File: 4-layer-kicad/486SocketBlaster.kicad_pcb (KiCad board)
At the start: 4 copper layers, 47.6 x 51.8 mm, 18 parts, among them U1 TPS563200

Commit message: update
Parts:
- added R4: 40.2K, 486SocketBlaster:R_0603_1608Metric, F.Cu at (130.6, 52.6)
- added RV1: 100K, 486SocketBlaster:tinySMDpot, F.Cu at (128.0, 46.2)
- R2: value 33.2K -> 68K
- moved C7 4.44 mm to (121.5, 44.2)
- moved C5 1.31 mm to (117.7, 44.2)
- moved C6 1.31 mm to (114.0, 44.2)
- moved C2 1.13 mm to (130.6, 62.3)
- moved L1 1.02 mm to (115.6, 55.1)
- moved R2 1.02 mm to (127.4, 52.6)
- moved R3 1.02 mm to (124.2, 52.6)
- moved C4 1.02 mm to (130.6, 57.7)
- moved R1 1.02 mm to (127.4, 57.7)
- moved U1 1.02 mm to (123.1, 57.7)
- moved C1 0.81 mm to (127.4, 62.3)
- moved C3 0.56 mm to (124.2, 62.3)
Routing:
- net Vin: track 15.9 -> 0.00 mm, vias 12 -> 6
- net Net-(RV1-Pad2): track 0.00 -> 5.18 mm
- net Vout: track 3.80 -> 8.05 mm, vias 8 -> 6
- net FBVoltage: track 10.6 -> 14.3 mm

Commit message: update
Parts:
- moved R4 15.8 mm to (115.2, 56.2)
- moved R2 15.7 mm to (112.1, 56.2)
- moved RV1 13.7 mm to (114.9, 50.2), turned to -90 degrees
- moved C2 12.8 mm to (117.9, 61.2)
- moved C1 12.8 mm to (114.7, 61.2)
- moved L1 9.99 mm to (125.5, 54.4)
- moved C7 9.78 mm to (131.3, 44.2)
- moved C5 9.78 mm to (127.5, 44.2)
- moved C6 9.78 mm to (123.8, 44.2)
- moved R3 6.79 mm to (118.5, 56.2)
- moved U1 4.49 mm to (125.5, 61.4), turned to -90 degrees
- moved C3 3.54 mm to (120.9, 61.2)
- moved R1 3.38 mm to (130.3, 55.9)
- moved C4 2.43 mm to (130.3, 60.1)
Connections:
- net Net-(RV1-Pad2) renamed /Trim
- C4 pad 1: SW -> Net-(U1-Pad6)
- C4 pad 2: Net-(C4-Pad2) -> /SW
- L1 pad 1: SW -> /SW
- R1 pad 1: Vin -> Net-(U1-Pad5)
- R1 pad 2: Net-(R1-Pad2) -> Vin
- R2 pad 1: FBVoltage -> /FBVoltage
- R3 pad 1: GND -> /FBVoltage
- R3 pad 2: FBVoltage -> GND
- R4 pad 1: FBVoltage -> /FBVoltage
- RV1 pad 1: Vout -> unconnected-(RV1-Pad1)
- RV1 pad 3: unconnected-(RV1-Pad3) -> Vout
- U1 pad 2: SW -> /SW
- U1 pad 4: FBVoltage -> /FBVoltage
- U1 pad 5: Net-(R1-Pad2) -> Net-(U1-Pad5)
- U1 pad 6: Net-(C4-Pad2) -> Net-(U1-Pad6)
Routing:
- net /FBVoltage: track 0.00 -> 28.0 mm
- net SW: track 24.6 -> 0.00 mm, vias 2 -> 0
- net Net-(U1-Pad5): track 0.00 -> 14.6 mm
- net FBVoltage: track 14.3 -> 0.00 mm, vias 2 -> 0
- net Net-(C4-Pad2): track 7.11 -> 0.00 mm
- net /SW: track 0.00 -> 6.05 mm
- net Net-(U1-Pad6): track 0.00 -> 5.04 mm
- net Vout: track 8.05 -> 4.26 mm, vias 6 -> 5
- net Net-(R1-Pad2): track 3.50 -> 0.00 mm
- net GND: track 8.60 -> 6.39 mm, vias 8 -> 10
- net Net-(Pins1-PadE3): track 3.68 -> 1.84 mm
- net Net-(Pins1-PadQ16): track 3.68 -> 1.84 mm
- net Net-(Pins1-PadQ14): track 3.53 -> 1.69 mm
- net Net-(Pins1-PadN16): track 3.68 -> 1.84 mm
- net Net-(Pins1-PadE15): track 3.68 -> 1.84 mm
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- added copper zone on F.Cu, net /SW
- added copper zone on B.Cu, net Vout
- removed copper zone on F.Cu, net SW
- removed copper zone on In1.Cu, net Vout

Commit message: update
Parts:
- added C8: 10uf, 486SocketBlaster:C_0805_2012Metric, F.Cu at (131.7, 44.1)
- added G***: LOGO, 486SocketBlaster:ScrapComputinglogo, B.Cu at (127.8, 58.7)
- added G***: LOGO, 486SocketBlaster:lime_logo_9mm, B.Cu at (114.9, 58.7)
- C3, C4: footprint 486SocketBlaster:C_0603_1608Metric -> 486SocketBlaster:C_0805_2012Metric
- C7: value 47uf -> 10uf; footprint 486SocketBlaster:CP_EIA-3216-12_Kemet-S_Pad1.58x1.35mm_HandSolder -> 486SocketBlaster:C_0805_2012Metric
- R2: value 68K -> 68.1K
- moved C7 10.9 mm to (120.4, 44.1)
- moved RV1 1.00 mm to (113.9, 50.2)
- moved C1 0.71 mm to (114.0, 61.2)
- moved C2 0.58 mm to (117.3, 61.2)
- moved C5 0.38 mm to (127.9, 44.2)
- moved C6 0.38 mm to (124.2, 44.2)
- moved C3 0.33 mm to (120.5, 61.2)
- moved Pins1 0.25 mm to (142.0, 31.8)
- renumbered CLKMUL1 to CLKMUL
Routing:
- net /FBVoltage: track 28.0 -> 23.6 mm
- net Vout: track 4.26 -> 3.85 mm, vias 5 -> 7
- net GND: track 6.39 -> 6.24 mm, vias 10 -> 11
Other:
- board text added: "/"
- board text added: "2.7v"
- board text added: "4.3v"
- board text added: "=>"
- board text added: "A"
- board text added: "Big Thanks:"
- board text added: "CalamityLime"
- board text added: "DX"
- board text added: "DX2"
- board text added: "N"
- board text added: "NC"
- board text added: "On-Board Regulator Edition"
- board text added: "On-Board Regulator:"
- board text added: "Original Design:"
- board text added: "OxCats"
- board text added: "SET BY MOTHERBOARD"
- board text added: "ScrapComputing"
- board text removed: "+"
- board text removed: "."
- board text removed: "DX/DX2"
- board text removed: "N/A"
- board text removed: "N/C"
- board text removed: "Set by Motherboard"
- board text removed: "by ScrapComputing"
- board text removed: "rev0.Lime"

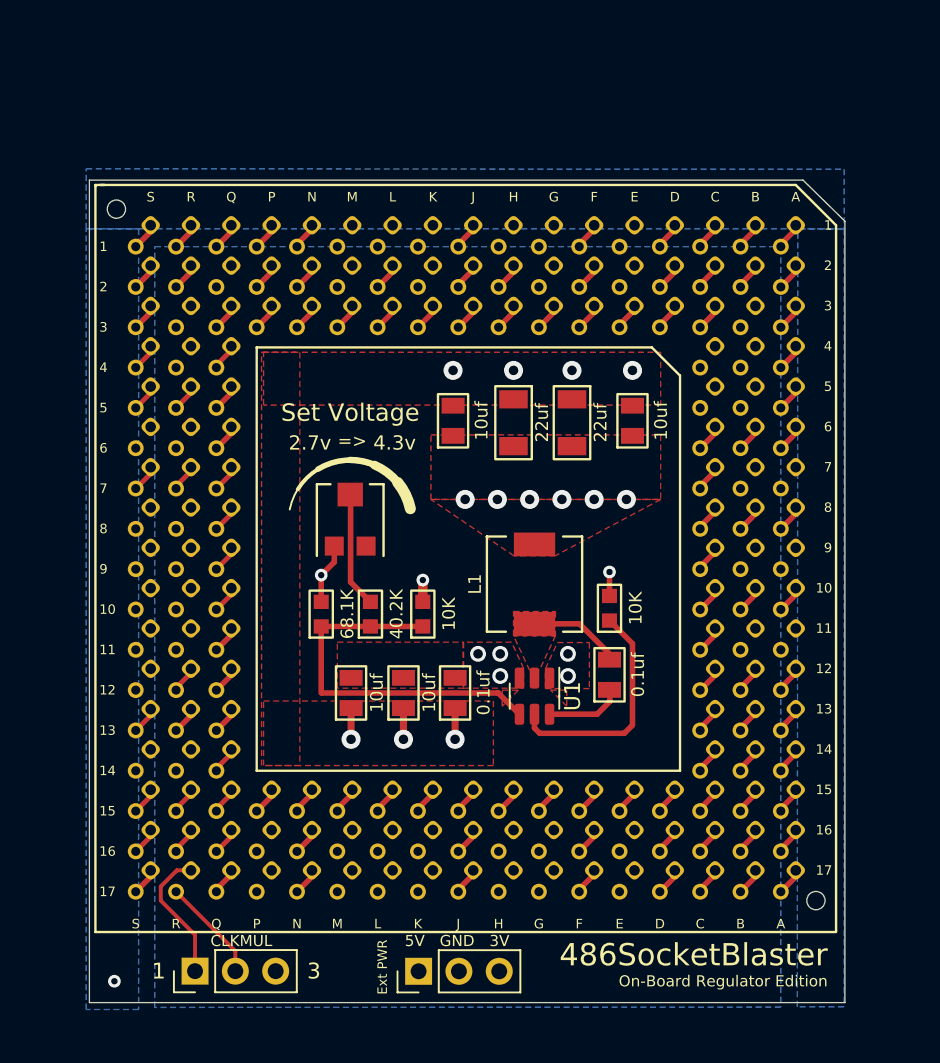
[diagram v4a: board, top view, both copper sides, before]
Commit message: update
+larger drill holes for socket
+Replaced 68.1K with 68K resistor, one less extended part from jlc
+updated gerbers, Bom & CPL
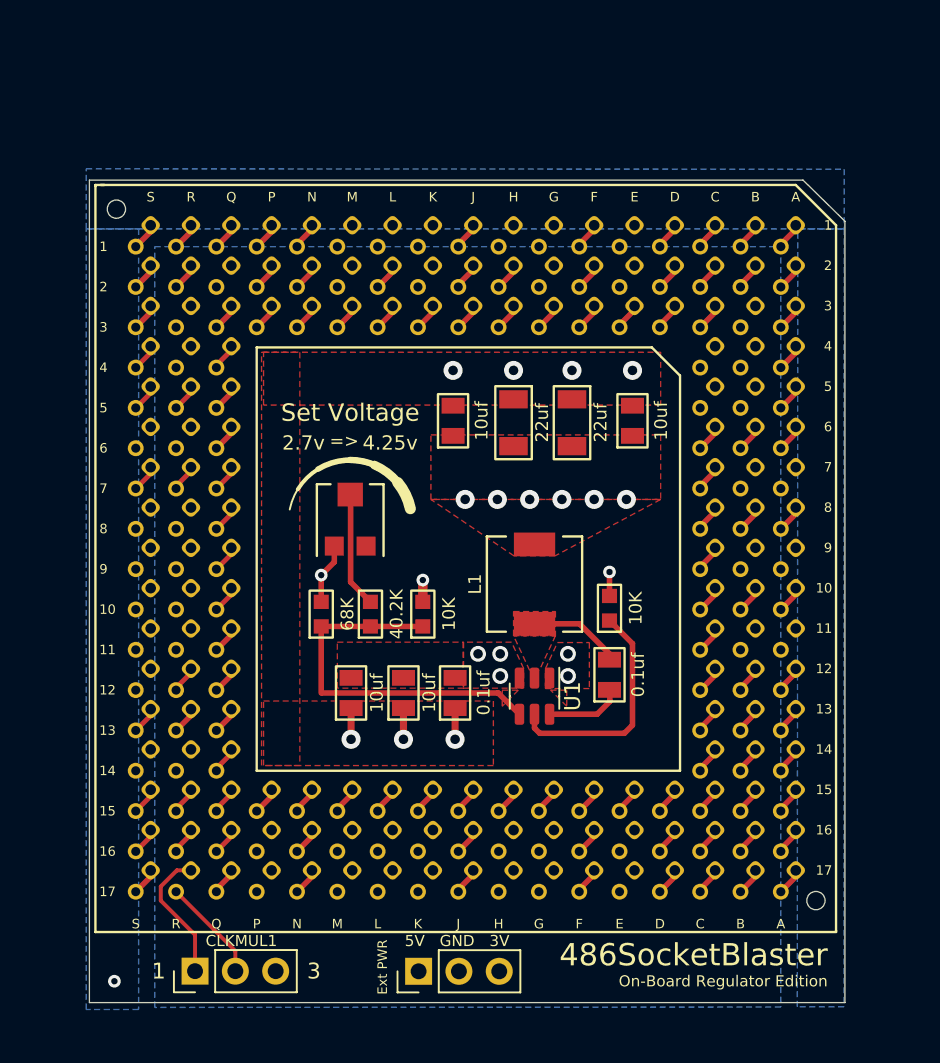
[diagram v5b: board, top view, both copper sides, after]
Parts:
- R2: value 68.1K -> 68K
- renumbered CLKMUL to CLKMUL1
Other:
- board text added: "4.25v"
- board text removed: "4.3v"
